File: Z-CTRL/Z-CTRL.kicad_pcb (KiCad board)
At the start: 2 copper layers, 60 x 60 mm, 56 parts, among them X1 SMA-F, X2 SMA-F, X3 SMA-F, X4 SMA-F

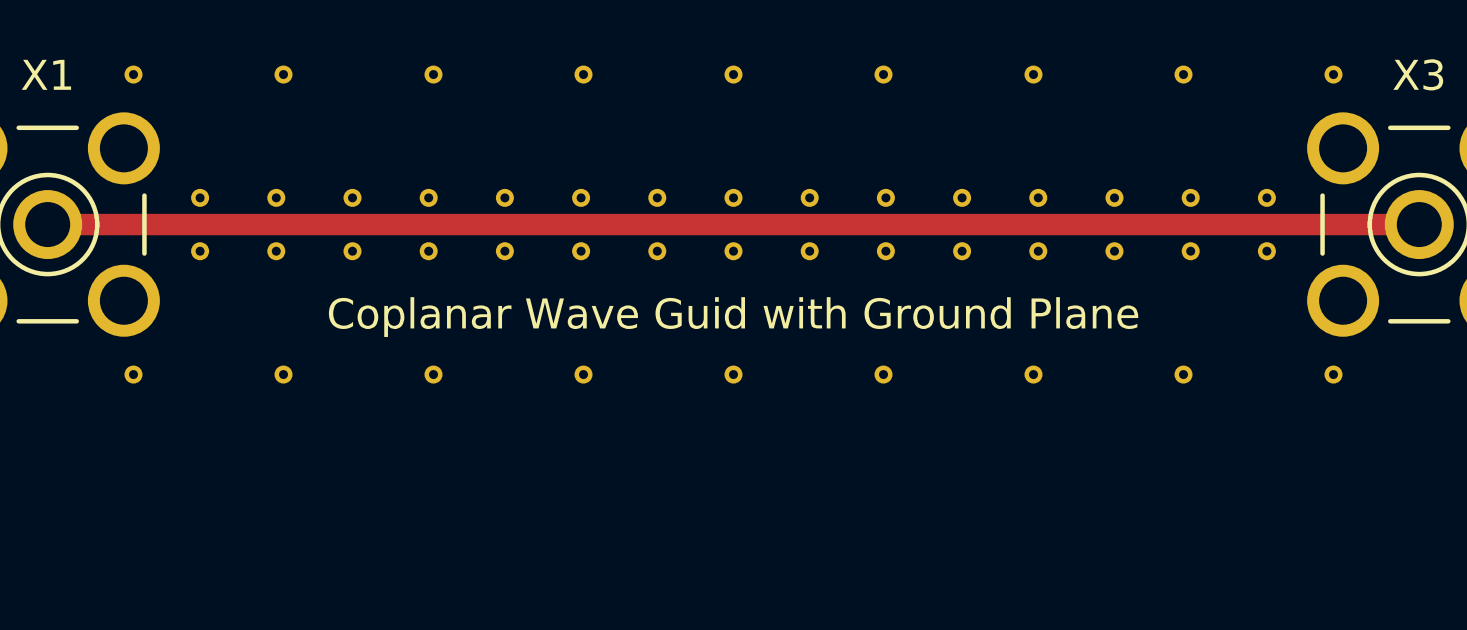
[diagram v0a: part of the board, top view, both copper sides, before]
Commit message: z-CTRL: Typo on silk screen
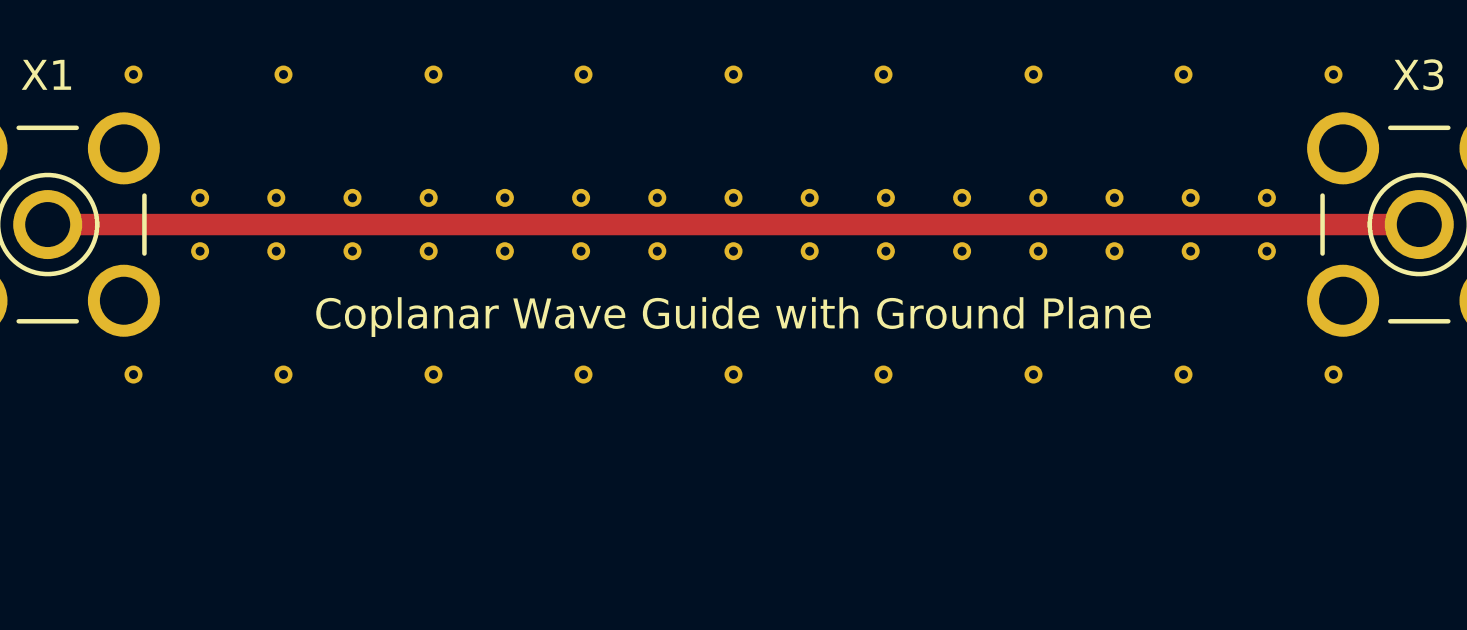
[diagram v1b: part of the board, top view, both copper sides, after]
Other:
- board text added: "Coplanar Wave Guide with Ground Plane"
- board text removed: "Coplanar Wave Guid with Ground Plane"
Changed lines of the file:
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@@
   (general
     (links 68)
-    (no_connects 52)
+    (no_connects 0)
     (area 89.326809 89.724999 185.693002 150.061001)
     (thickness 1.6)
@@
       (net 4 "Net-(X2-PadHF)") (zone_connect 1))
   )
-  (gr_text "Coplanar Wave Guid with Ground Plane" (at 120.028 107.986) (layer F.SilkS)
+  (gr_text "Coplanar Wave Guide with Ground Plane" (at 120.028 107.986) (layer F.SilkS)
     (effects (font (size 1 1) (thickness 0.15)))
   )
